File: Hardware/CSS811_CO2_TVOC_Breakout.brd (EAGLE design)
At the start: 55.9 x 34.3 mm, 19 parts, among them U2 CCS811PRODUCTION

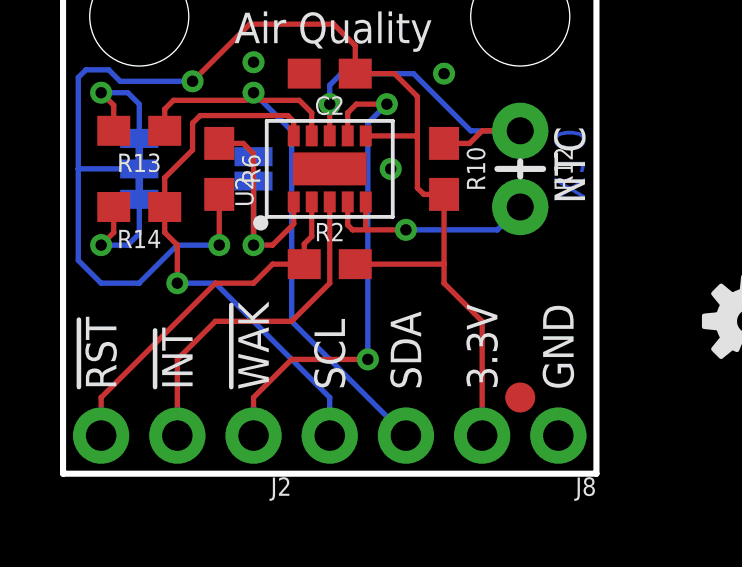
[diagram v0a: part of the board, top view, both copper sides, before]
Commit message: Adding panel and removing extraneous files.
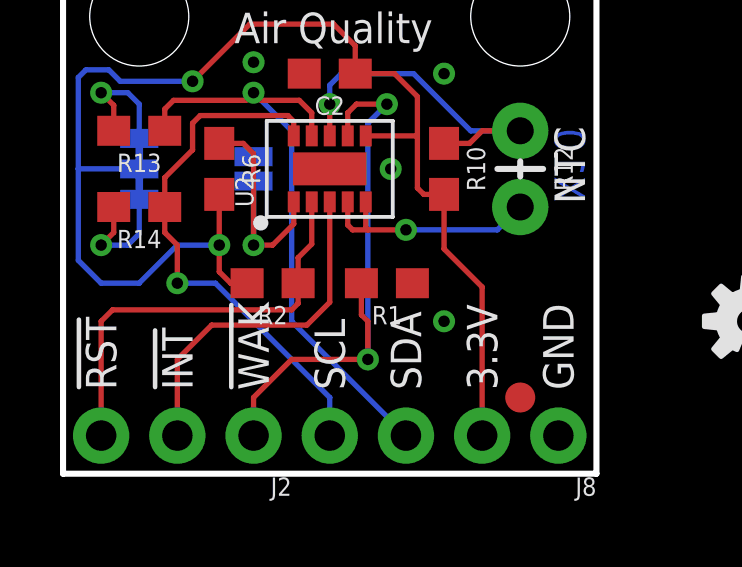
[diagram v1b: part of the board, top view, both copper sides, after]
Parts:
- added R1: 100k, SparkFun-Resistors:0603
- moved R2 2.01 mm to (6.99, 6.35), turned to 180 degrees
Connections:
- net !WAKE: now also R1.2
- net GND: now also R1.1
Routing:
- net !WAKE: track 16.6 -> 19.2 mm
- net !RST: track 12.1 -> 14.2 mm
- net 3.3V: track 46.5 -> 45.6 mm
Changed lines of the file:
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@@
 <?xml version="1.0" encoding="utf-8"?>
 <!DOCTYPE eagle SYSTEM "eagle.dtd">
-<eagle version="7.5.0">
+<eagle version="7.7.0">
 <drawing>
 <settings>
@@
 <layer number="20" name="Dimension" color="15" fill="1" visible="yes" active="yes"/>
 <layer number="21" name="tPlace" color="16" fill="1" visible="yes" active="yes"/>
-<layer number="22" name="bPlace" color="14" fill="1" visible="yes" active="yes"/>
+<layer number="22" name="bPlace" color="14" fill="1" visible="no" active="yes"/>
 <layer number="23" name="tOrigins" color="15" fill="1" visible="yes" active="yes"/>
-<layer number="24" name="bOrigins" color="15" fill="1" visible="yes" active="yes"/>
-<layer number="25" name="tNames" color="7" fill="1" visible="no" active="yes"/>
+<layer number="24" name="bOrigins" color="15" fill="1" visible="no" active="yes"/>
+<layer number="25" name="tNames" color="7" fill="1" visible="yes" active="yes"/>
 <layer number="26" name="bNames" color="7" fill="1" visible="no" active="yes"/>
 <layer number="27" name="tValues" color="7" fill="1" visible="no" active="yes"/>
@@
 <layer number="43" name="vRestrict" color="2" fill="10" visible="no" active="yes"/>
 <layer number="44" name="Drills" color="7" fill="1" visible="no" active="yes"/>
-<layer number="45" name="Holes" color="7" fill="1" visible="yes" active="yes"/>
+<layer number="45" name="Holes" color="7" fill="1" visible="no" active="yes"/>
 <layer number="46" name="Milling" color="3" fill="1" visible="no" active="yes"/>
 <layer number="47" name="Measures" color="7" fill="1" visible="no" active="yes"/>
 <layer number="48" name="Document" color="7" fill="1" visible="no" active="yes"/>
-<layer number="49" name="Reference" color="7" fill="1" visible="yes" active="yes"/>
+<layer number="49" name="Reference" color="7" fill="1" visible="no" active="yes"/>
 <layer number="50" name="dxf" color="7" fill="1" visible="no" active="no"/>
-<layer number="51" name="tDocu" color="6" fill="1" visible="yes" active="yes"/>
+<layer number="51" name="tDocu" color="6" fill="1" visible="no" active="yes"/>
 <layer number="52" name="bDocu" color="7" fill="1" visible="no" active="yes"/>
 <layer number="53" name="tGND_GNDA" color="7" fill="9" visible="no" active="no"/>
@@
 <element name="FD1" library="SparkFun-Aesthetics" package="FIDUCIAL-1X2" value="FIDUCIAL1X2" x="0.762" y="17.018"/>
 <element name="FD2" library="SparkFun-Aesthetics" package="FIDUCIAL-1X2" value="FIDUCIAL1X2" x="15.24" y="2.54"/>
-<element name="R2" library="SparkFun-Resistors" package="0603" value="4.7k" x="8.89" y="6.985">
-<attribute name="PROD_ID" value="RES-07857" x="8.89" y="6.985" size="1.778" layer="27" font="vector" ratio="15" display="off"/>
+<element name="R2" library="SparkFun-Resistors" package="0603" value="4.7k" x="6.985" y="6.35" rot="R180">
+<attribute name="PROD_ID" value="RES-07857" x="6.985" y="6.35" size="1.778" layer="27" font="vector" ratio="15" rot="R180" display="off"/>
 </element>
 <element name="U$1" library="SparkX" package="SPARKX-SMALL" value="SPARKX-LOGO3" x="8.89" y="15.24" rot="MR0"/>
 <element name="J2" library="SparkFun-Connectors" package="1X03_NO_SILK" value="" x="6.35" y="1.27" rot="R180"/>
 <element name="U2" library="SparkX" package="LGA10" value="CCS811PRODUCTION" x="8.89" y="10.16" rot="R90"/>
+<element name="R1" library="SparkFun-Resistors" package="0603" value="100k" x="10.795" y="6.35" rot="R180">
+<attribute name="PROD_ID" value="RES-07828" x="10.795" y="6.35" size="1.778" layer="27" font="vector" ratio="15" rot="R180" display="off"/>
+</element>
 </elements>
 <signals>
@@
 <via x="10.922" y="10.16" extent="1-16" drill="0.381"/>
 <via x="12.7" y="13.335" extent="1-16" drill="0.381"/>
+<contactref element="R1" pad="1"/>
+<via x="12.7" y="5.08" extent="1-16" drill="0.381"/>
 </signal>
 <signal name="SCL">
@@
 <contactref element="JP1" pad="2"/>
 <contactref element="R2" pad="2"/>
-<wire x1="13.97" y1="1.27" x2="13.97" y2="5.08" width="0.1778" layer="1"/>
-<wire x1="13.97" y1="5.08" x2="12.7" y2="6.35" width="0.1778" layer="1"/>
-<wire x1="12.7" y1="6.35" x2="12.7" y2="6.985" width="0.1778" layer="1"/>
-<wire x1="12.7" y1="6.985" x2="12.7" y2="9.31" width="0.1778" layer="1"/>
-<wire x1="9.74" y1="6.985" x2="12.7" y2="6.985" width="0.1778" layer="1"/>
+<wire x1="13.97" y1="1.27" x2="13.97" y2="6.223" width="0.1778" layer="1"/>
+<wire x1="13.97" y1="6.223" x2="12.7" y2="7.493" width="0.1778" layer="1"/>
+<wire x1="12.7" y1="7.493" x2="12.7" y2="9.31" width="0.1778" layer="1"/>
 <wire x1="11.049" y1="13.335" x2="9.74" y2="13.335" width="0.1778" layer="1"/>
 <wire x1="6.223" y1="14.986" x2="9.017" y2="14.986" width="0.1778" layer="1"/>
@@
 <wire x1="11.811" y1="12.573" x2="11.049" y2="13.335" width="0.1778" layer="1"/>
 <wire x1="11.768" y1="11.26" x2="11.811" y2="11.303" width="0.1778" layer="1"/>
+<wire x1="6.135" y1="6.35" x2="5.588" y2="6.35" width="0.1778" layer="1"/>
+<wire x1="5.588" y1="6.35" x2="5.207" y2="6.731" width="0.1778" layer="1"/>
+<wire x1="5.207" y1="6.731" x2="5.207" y2="7.62" width="0.1778" layer="1"/>
 </signal>
 <signal name="!RST">
 <contactref element="R2" pad="1"/>
 <contactref element="J2" pad="3"/>
-<wire x1="8.29" y1="7.909" x2="8.04" y2="7.659" width="0.1778" layer="1"/>
-<wire x1="8.04" y1="6.985" x2="8.04" y2="7.659" width="0.1778" layer="1"/>
 <contactref element="U2" pad="2"/>
-<wire x1="8.29" y1="9.06" x2="8.29" y2="7.909" width="0.1778" layer="1"/>
-<wire x1="8.04" y1="6.985" x2="6.985" y2="6.985" width="0.1778" layer="1"/>
-<wire x1="6.985" y1="6.985" x2="6.35" y2="6.35" width="0.1778" layer="1"/>
-<wire x1="6.35" y1="6.35" x2="5.08" y2="6.35" width="0.1778" layer="1"/>
-<wire x1="5.08" y1="6.35" x2="1.27" y2="2.54" width="0.1778" layer="1"/>
-<wire x1="1.27" y1="2.54" x2="1.27" y2="1.27" width="0.1778" layer="1"/>
+<wire x1="8.29" y1="9.06" x2="8.29" y2="7.655" width="0.1778" layer="1"/>
+<wire x1="8.29" y1="7.655" x2="7.835" y2="7.2" width="0.1778" layer="1"/>
+<wire x1="7.835" y1="6.35" x2="7.835" y2="7.2" width="0.1778" layer="1"/>
+<wire x1="7.835" y1="6.35" x2="7.835" y2="5.676" width="0.1778" layer="1"/>
+<wire x1="7.835" y1="5.676" x2="7.62" y2="5.461" width="0.1778" layer="1"/>
+<wire x1="7.62" y1="5.461" x2="1.651" y2="5.461" width="0.1778" layer="1"/>
+<wire x1="1.651" y1="5.461" x2="1.27" y2="5.08" width="0.1778" layer="1"/>
+<wire x1="1.27" y1="5.08" x2="1.27" y2="1.27" width="0.1778" layer="1"/>
 </signal>
 <signal name="CCS811_ADDR">
@@
 <signal name="!INT">
 <contactref element="J2" pad="2"/>
-<wire x1="8.89" y1="6.35" x2="7.62" y2="5.08" width="0.1778" layer="1"/>
-<wire x1="7.62" y1="5.08" x2="5.08" y2="5.08" width="0.1778" layer="1"/>
-<wire x1="5.08" y1="5.08" x2="3.81" y2="3.81" width="0.1778" layer="1"/>
+<contactref element="U2" pad="3"/>
+<wire x1="8.89" y1="9.06" x2="8.89" y2="5.715" width="0.1778" layer="1"/>
+<wire x1="8.89" y1="5.715" x2="8.128" y2="4.953" width="0.1778" layer="1"/>
+<wire x1="8.128" y1="4.953" x2="4.953" y2="4.953" width="0.1778" layer="1"/>
+<wire x1="4.953" y1="4.953" x2="3.81" y2="3.81" width="0.1778" layer="1"/>
 <wire x1="3.81" y1="3.81" x2="3.81" y2="1.27" width="0.1778" layer="1"/>
-<contactref element="U2" pad="3"/>
-<wire x1="8.89" y1="9.06" x2="8.89" y2="6.35" width="0.1778" layer="1"/>
 </signal>
 <signal name="!WAKE">
@@
 <wire x1="10.16" y1="3.81" x2="10.16" y2="11.684" width="0.1778" layer="16"/>
 <wire x1="10.16" y1="11.684" x2="10.795" y2="12.319" width="0.1778" layer="16"/>
+<contactref element="R1" pad="2"/>
+<wire x1="9.945" y1="6.35" x2="9.945" y2="5.295" width="0.1778" layer="1"/>
+<wire x1="9.945" y1="5.295" x2="10.16" y2="5.08" width="0.1778" layer="1"/>
+<wire x1="10.16" y1="5.08" x2="10.16" y2="3.81" width="0.1778" layer="1"/>
 </signal>
 <signal name="NTC_SENSE">

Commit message: Reviewed and fixed Panel
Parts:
- moved LOGO4 14.2 mm to (8.89, 7.62), flipped to the bottom
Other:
- board text added: "ADDR"
- board text added: "I2C PU"
- board text removed: "JP1"
- board text removed: "JP2"
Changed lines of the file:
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@@
 <?xml version="1.0" encoding="utf-8"?>
 <!DOCTYPE eagle SYSTEM "eagle.dtd">
-<eagle version="7.7.0">
+<eagle version="7.6.0">
 <drawing>
 <settings>
@@
 <layer number="20" name="Dimension" color="15" fill="1" visible="yes" active="yes"/>
 <layer number="21" name="tPlace" color="16" fill="1" visible="yes" active="yes"/>
-<layer number="22" name="bPlace" color="14" fill="1" visible="no" active="yes"/>
+<layer number="22" name="bPlace" color="14" fill="1" visible="yes" active="yes"/>
 <layer number="23" name="tOrigins" color="15" fill="1" visible="yes" active="yes"/>
-<layer number="24" name="bOrigins" color="15" fill="1" visible="no" active="yes"/>
-<layer number="25" name="tNames" color="7" fill="1" visible="yes" active="yes"/>
+<layer number="24" name="bOrigins" color="15" fill="1" visible="yes" active="yes"/>
+<layer number="25" name="tNames" color="7" fill="1" visible="no" active="yes"/>
 <layer number="26" name="bNames" color="7" fill="1" visible="no" active="yes"/>
 <layer number="27" name="tValues" color="7" fill="1" visible="no" active="yes"/>
@@
 <layer number="43" name="vRestrict" color="2" fill="10" visible="no" active="yes"/>
 <layer number="44" name="Drills" color="7" fill="1" visible="no" active="yes"/>
-<layer number="45" name="Holes" color="7" fill="1" visible="no" active="yes"/>
+<layer number="45" name="Holes" color="7" fill="1" visible="yes" active="yes"/>
 <layer number="46" name="Milling" color="3" fill="1" visible="no" active="yes"/>
 <layer number="47" name="Measures" color="7" fill="1" visible="no" active="yes"/>
 <layer number="48" name="Document" color="7" fill="1" visible="no" active="yes"/>
-<layer number="49" name="Reference" color="7" fill="1" visible="no" active="yes"/>
+<layer number="49" name="Reference" color="7" fill="1" visible="yes" active="yes"/>
 <layer number="50" name="dxf" color="7" fill="1" visible="no" active="no"/>
-<layer number="51" name="tDocu" color="6" fill="1" visible="no" active="yes"/>
+<layer number="51" name="tDocu" color="6" fill="1" visible="yes" active="yes"/>
 <layer number="52" name="bDocu" color="7" fill="1" visible="no" active="yes"/>
 <layer number="53" name="tGND_GNDA" color="7" fill="9" visible="no" active="no"/>
@@
 <text x="9.017" y="16.51" size="1.2065" layer="21" ratio="15" align="center">CCS811</text>
 <text x="17.399" y="10.287" size="1.016" layer="16" ratio="20" rot="MR270" align="bottom-center">X10</text>
-<text x="4.191" y="10.287" size="0.889" layer="22" ratio="15" rot="MR90" align="bottom-center">JP2</text>
+<text x="4.191" y="10.287" size="0.889" layer="22" ratio="15" rot="MR90" align="bottom-center">ADDR</text>
 <text x="16.51" y="-21.59" size="1.778" layer="51">Jim Lindblom</text>
 <dimension x1="0" y1="0" x2="0" y2="50.8" x3="-15.24" y3="25.4" textsize="0.889" textratio="15" layer="47" dtype="vertical" unit="inch" precision="3"/>
@@
 <text x="17.399" y="10.287" size="1.016" layer="21" ratio="15" rot="R90" align="bottom-center">NTC</text>
 <text x="9.017" y="14.859" size="1.016" layer="21" ratio="15" align="center">Air Quality</text>
-<text x="0.381" y="10.287" size="0.889" layer="22" ratio="15" rot="MR90" align="bottom-center">JP1</text>
+<text x="0.381" y="10.287" size="0.889" layer="22" ratio="15" rot="MR90" align="bottom-center">I2C PU</text>
 <text x="6.35" y="2.794" size="1.016" layer="21" font="vector" ratio="15" rot="R90" align="center-left">!WAK</text>
 <text x="3.81" y="2.794" size="1.016" layer="21" font="vector" ratio="15" rot="R90" align="center-left">!INT</text>
@@
 <attribute name="SF_ID" value="SEN-00250" x="15.24" y="10.16" size="1.778" layer="27" rot="R270" display="off"/>
 </element>
-<element name="LOGO4" library="SparkFun-Aesthetics" package="OSHW-LOGO-S" value="OSHW-LOGOS" x="22.86" y="5.08"/>
+<element name="LOGO4" library="SparkFun-Aesthetics" package="OSHW-LOGO-S" value="OSHW-LOGOS" x="8.89" y="7.62" rot="MR0"/>
 <element name="FD1" library="SparkFun-Aesthetics" package="FIDUCIAL-1X2" value="FIDUCIAL1X2" x="0.762" y="17.018"/>
 <element name="FD2" library="SparkFun-Aesthetics" package="FIDUCIAL-1X2" value="FIDUCIAL1X2" x="15.24" y="2.54"/>
